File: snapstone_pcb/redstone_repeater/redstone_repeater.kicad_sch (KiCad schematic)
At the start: 17 parts, among them SW1 SW_Push, SW2 SW_Push, SW3 SW_Push, SW4 SW_Push, U1 MOUDLE-SEEEDUINO-XIAO, U2 Current Sensor

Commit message: Added almost all footprints
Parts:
- R1, R2, R3, R4, R5: footprint (none) -> Resistor_THT:R_Axial_DIN0309_L9.0mm_D3.2mm_P25.40mm_Horizontal
- SW1, SW2, SW3, SW4: footprint (none) -> Button_Switch_Keyboard:SW_Cherry_MX_1.00u_PCB
- U1: footprint (none) -> footprints:XIAO-Generic-Hybrid-14P-2.54-21X17.8MM
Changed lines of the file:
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@@
 			)
 		)
-		(property "Footprint" ""
+		(property "Footprint" "Resistor_THT:R_Axial_DIN0309_L9.0mm_D3.2mm_P25.40mm_Horizontal"
 			(at 193.294 84.074 90)
 			(effects
@@
 			)
 		)
-		(property "Footprint" ""
+		(property "Footprint" "Resistor_THT:R_Axial_DIN0309_L9.0mm_D3.2mm_P25.40mm_Horizontal"
 			(at 193.294 103.124 90)
 			(effects
@@
 			)
 		)
-		(property "Footprint" ""
+		(property "Footprint" "Resistor_THT:R_Axial_DIN0309_L9.0mm_D3.2mm_P25.40mm_Horizontal"
 			(at 193.294 65.024 90)
 			(effects
@@
 			)
 		)
-		(property "Footprint" ""
+		(property "Footprint" "Button_Switch_Keyboard:SW_Cherry_MX_1.00u_PCB"
 			(at 180.34 80.01 0)
 			(effects
@@
 			)
 		)
-		(property "Footprint" ""
+		(property "Footprint" "footprints:XIAO-Generic-Hybrid-14P-2.54-21X17.8MM"
 			(at 101.6 109.22 0)
 			(effects
@@
 			)
 		)
-		(property "Footprint" ""
+		(property "Footprint" "Resistor_THT:R_Axial_DIN0309_L9.0mm_D3.2mm_P25.40mm_Horizontal"
 			(at 119.126 72.136 90)
 			(effects
@@
 			)
 		)
-		(property "Footprint" ""
+		(property "Footprint" "Button_Switch_Keyboard:SW_Cherry_MX_1.00u_PCB"
 			(at 180.34 118.11 0)
 			(effects
@@
 			)
 		)
-		(property "Footprint" ""
+		(property "Footprint" "Resistor_THT:R_Axial_DIN0309_L9.0mm_D3.2mm_P25.40mm_Horizontal"
 			(at 193.294 122.174 90)
 			(effects
@@
 			)
 		)
-		(property "Footprint" ""
+		(property "Footprint" "Button_Switch_Keyboard:SW_Cherry_MX_1.00u_PCB"
 			(at 180.34 60.96 0)
 			(effects
@@
 			)
 		)
-		(property "Footprint" ""
+		(property "Footprint" "Button_Switch_Keyboard:SW_Cherry_MX_1.00u_PCB"
 			(at 180.34 99.06 0)
 			(effects

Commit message: All fottprints done schematic should be done
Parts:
- C1, C2, C3, C4: footprint (none) -> Capacitor_THT:CP_Radial_Tantal_D5.0mm_P2.50mm
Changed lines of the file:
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@@
 			)
 		)
-		(property "Footprint" ""
+		(property "Footprint" "Capacitor_THT:CP_Radial_Tantal_D5.0mm_P2.50mm"
 			(at 209.55 84.1248 0)
 			(effects
@@
 			)
 		)
-		(property "Footprint" ""
+		(property "Footprint" "Capacitor_THT:CP_Radial_Tantal_D5.0mm_P2.50mm"
 			(at 209.55 122.2248 0)
 			(effects
@@
 			)
 		)
-		(property "Footprint" ""
+		(property "Footprint" "Capacitor_THT:CP_Radial_Tantal_D5.0mm_P2.50mm"
 			(at 209.55 103.1748 0)
 			(effects
@@
 			)
 		)
-		(property "Footprint" ""
+		(property "Footprint" "Capacitor_THT:CP_Radial_Tantal_D5.0mm_P2.50mm"
 			(at 209.55 65.0748 0)
 			(effects

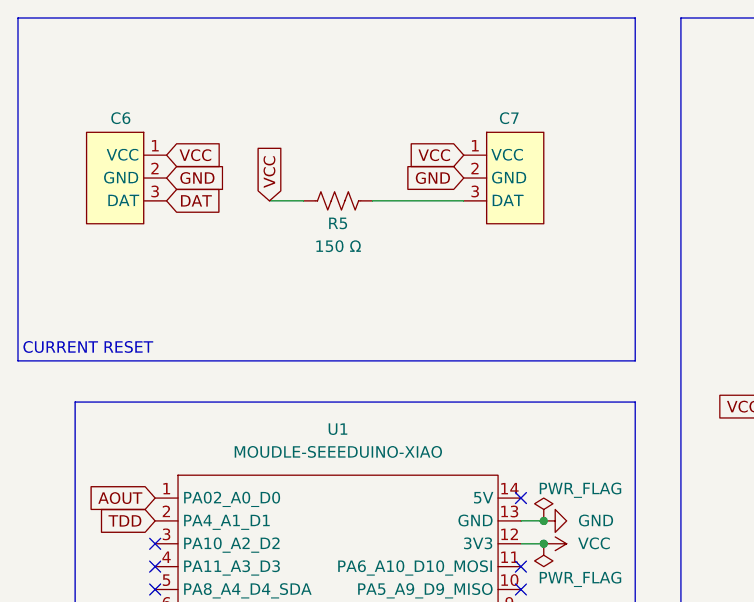
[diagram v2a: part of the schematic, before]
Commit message: Rerouted comparator wires to loop back into connector for inputs #1 and #2... and made some tiny style changes, lol.
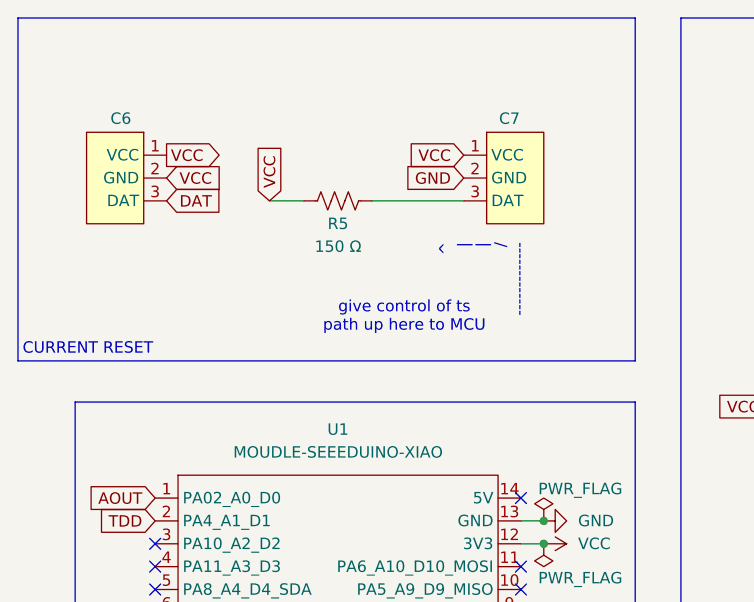
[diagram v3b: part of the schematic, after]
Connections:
- net GND: no longer C6.2 (GND)
- net VCC: now also C6.2 (GND)
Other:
- note added: "^ | | / -------------"
- note added: "give control of ts path up here to MCU"
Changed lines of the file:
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@@
+		)
+	)
+	(text "^\n|\n|\n/\n-------------  "
+		(exclude_from_sim no)
+		(at 135.382 75.946 90)
+		(effects
+			(font
+				(size 1.27 1.27)
+			)
+			(justify right)
 		)
 	)
@@
 		)
 	)
+	(text "give control of ts\npath up here to MCU"
+		(exclude_from_sim no)
+		(at 126.746 84.074 0)
+		(effects
+			(font
+				(size 1.27 1.27)
+			)
+		)
+	)
 	(text "MCU"
 		(exclude_from_sim no)
@@
 		)
 	)
+	(global_label "VCC"
+		(shape input)
+		(at 100.33 68.58 0)
+		(fields_autoplaced yes)
+		(effects
+			(font
+				(size 1.27 1.27)
+			)
+			(justify left)
+		)
+		(property "Intersheetrefs" "${INTERSHEET_REFS}"
+			(at 106.9438 68.58 0)
+			(effects
+				(font
+					(size 1.27 1.27)
+				)
+				(justify left)
+				(hide yes)
+			)
+		)
+	)
 	(global_label "TDD"
 		(shape input)
@@
 	)
 	(global_label "VCC"
-		(shape input)
+		(shape output)
 		(at 100.33 66.04 0)
 		(fields_autoplaced yes)
@@
 				(hide yes)
 			)
-		)
-	)
-	(global_label "GND"
-		(shape input)
-		(at 100.33 68.58 0)
-		(fields_autoplaced yes)
-		(effects
-			(font
-				(size 1.27 1.27)
-			)
-			(justify left)
-		)
-		(property "Intersheetrefs" "${INTERSHEET_REFS}"
-			(at 107.1857 68.58 0)
-			(effects
-				(font
-					(size 1.27 1.27)
-				)
-				(justify left)
-				(hide yes)
-			)

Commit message: Finished footprints and did all pcb in 30 mins somehow :sob:
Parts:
- C6, C7: footprint (none) -> TerminalBlock_4Ucon:TerminalBlock_4Ucon_1x03_P3.50mm_Horizontal
- U2: footprint TMCS1108A2UQDR_Current_Sensor:D0008A-IPC_A -> CurrentSensorSnap:D0008A-IPC_B
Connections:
- net DAT: now also U1.3 (PA10_A2_D2)
- net GND: no longer U2.4 (IN-)
- no-connect marks 13 -> 12
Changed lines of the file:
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@@
-	)
-	(no_connect
-		(at 99.06 109.22)
 	)
 	(no_connect
@@
 		(pts
 			(xy 185.42 85.09) (xy 189.23 85.09)
-		)
-		(stroke
-			(width 0)
-			(type default)
-		)
-	)
-	(wire
-		(pts
-			(xy 140.97 149.86) (xy 143.51 149.86)
 		)
 		(stroke
@@
 		)
 	)
-	(global_label "GND"
-		(shape input)
-		(at 105.41 160.02 180)
+	(global_label "TDD"
+		(shape output)
+		(at 199.39 69.85 270)
 		(fields_autoplaced yes)
 		(effects
@@
 		)
 		(property "Intersheetrefs" "${INTERSHEET_REFS}"
-			(at 98.5543 160.02 0)
+			(at 199.39 76.3428 90)
 			(effects
 				(font
@@
 		)
 	)
-	(global_label "TDD"
+	(global_label "VCC"
 		(shape output)
-		(at 199.39 69.85 270)
+		(at 100.33 66.04 0)
 		(fields_autoplaced yes)
 		(effects
@@
 				(size 1.27 1.27)
 			)
-			(justify right)
+			(justify left)
 		)
 		(property "Intersheetrefs" "${INTERSHEET_REFS}"
-			(at 199.39 76.3428 90)
-			(effects
-				(font
-					(size 1.27 1.27)
-				)
-				(justify right)
-				(hide yes)
-			)
-		)
-	)
-	(global_label "VCC"
-		(shape output)
-		(at 100.33 66.04 0)
+			(at 106.9438 66.04 0)
+			(effects
+				(font
+					(size 1.27 1.27)
+				)
+				(justify left)
+				(hide yes)
+			)
+		)
+	)
+	(global_label "AOUT"
+		(shape input)
+		(at 99.06 104.14 180)
 		(fields_autoplaced yes)
 		(effects
@@
 				(size 1.27 1.27)
 			)
-			(justify left)
+			(justify right)
 		)
 		(property "Intersheetrefs" "${INTERSHEET_REFS}"
-			(at 106.9438 66.04 0)
-			(effects
-				(font
-					(size 1.27 1.27)
-				)
-				(justify left)
-				(hide yes)
-			)
-		)
-	)
-	(global_label "AOUT"
+			(at 91.3576 104.14 0)
+			(effects
+				(font
+					(size 1.27 1.27)
+				)
+				(justify right)
+				(hide yes)
+			)
+		)
+	)
+	(global_label "VCC"
 		(shape input)
-		(at 99.06 104.14 180)
+		(at 167.64 93.98 180)
 		(fields_autoplaced yes)
 		(effects
@@
 		)
 		(property "Intersheetrefs" "${INTERSHEET_REFS}"
-			(at 91.3576 104.14 0)
+			(at 161.0262 93.98 0)
 			(effects
 				(font
@@
 		)
 	)
-	(global_label "VCC"
+	(global_label "DAT"
 		(shape input)
-		(at 167.64 93.98 180)
+		(at 105.41 144.78 180)
 		(fields_autoplaced yes)
 		(effects
@@
 		)
 		(property "Intersheetrefs" "${INTERSHEET_REFS}"
-			(at 161.0262 93.98 0)
+			(at 99.0986 144.78 0)
 			(effects
 				(font
@@
 		)
 	)
-	(global_label "DAT"
-		(shape input)
-		(at 105.41 144.78 180)
+	(global_label "TDD"
+		(shape output)
+		(at 199.39 127 270)
 		(fields_autoplaced yes)
 		(effects
@@
 		)
 		(property "Intersheetrefs" "${INTERSHEET_REFS}"
-			(at 99.0986 144.78 0)
+			(at 199.39 133.4928 90)
 			(effects
 				(font
@@
 		)
 	)
-	(global_label "TDD"
-		(shape output)
-		(at 199.39 127 270)
+	(global_label "DAT"
+		(shape input)
+		(at 99.06 109.22 180)
 		(fields_autoplaced yes)
 		(effects
@@
 		)
 		(property "Intersheetrefs" "${INTERSHEET_REFS}"
-			(at 199.39 133.4928 90)
+			(at 92.7486 109.22 0)
 			(effects
 				(font
@@
 	(global_label "AOUT"
 		(shape output)
-		(at 143.51 149.86 0)
+		(at 140.97 149.86 0)
 		(fields_autoplaced yes)
 		(effects
@@
 		)
 		(property "Intersheetrefs" "${INTERSHEET_REFS}"
-			(at 151.2124 149.86 0)
+			(at 148.6724 149.86 0)
 			(effects
 				(font
@@
 			)
 		)
-		(property "Footprint" ""
+		(property "Footprint" "TerminalBlock_4Ucon:TerminalBlock_4Ucon_1x03_P3.50mm_Horizontal"
 			(at 138.43 73.66 0)
 			(effects
@@
 			)
 		)
-		(property "Footprint" ""
+		(property "Footprint" "TerminalBlock_4Ucon:TerminalBlock_4Ucon_1x03_P3.50mm_Horizontal"
 			(at 95.25 73.66 0)
 			(effects
@@
 			)
 		)
-		(property "Footprint" "TMCS1108A2UQDR_Current_Sensor:D0008A-IPC_A"
+		(property "Footprint" "CurrentSensorSnap:D0008A-IPC_B"
 			(at 105.41 144.78 0)
 			(effects

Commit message: did a bunch of stuff (something something Redstone Repeater PCB Changes)
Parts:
- C_IN1: renamed from C6; footprint TerminalBlock_4Ucon:TerminalBlock_4Ucon_1x03_P3.50mm_Horizontal -> 691137710003_Board_To_Wire:691137710003_Board_To_Wire
- C_OUT1: renamed from C7; footprint TerminalBlock_4Ucon:TerminalBlock_4Ucon_1x03_P3.50mm_Horizontal -> 691137710003_Board_To_Wire:691137710003_Board_To_Wire
- R1, R2, R3, R4, R5: footprint Resistor_THT:R_Axial_DIN0309_L9.0mm_D3.2mm_P25.40mm_Horizontal -> CF12JT150R_Resistor_150:STA_CF12_STP
- U2: footprint CurrentSensorSnap:D0008A-IPC_B -> TMCS1108A2UQDR_Current_Sensor:D0008A-IPC_A
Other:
- note removed: "^ | | / -------------"
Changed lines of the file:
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@@
-		)
-	)
-	(text "^\n|\n|\n/\n-------------  "
-		(exclude_from_sim no)
-		(at 135.382 75.946 90)
-		(effects
-			(font
-				(size 1.27 1.27)
-			)
-			(justify right)
 		)
 	)
@@
 		(on_board yes)
 		(dnp no)
-		(property "Reference" "C7"
-			(at 138.43 61.976 0)
+		(property "Reference" "C_OUT1"
+			(at 139.192 61.722 0)
 			(effects
 				(font
@@
 			)
 		)
-		(property "Footprint" "TerminalBlock_4Ucon:TerminalBlock_4Ucon_1x03_P3.50mm_Horizontal"
+		(property "Footprint" "691137710003_Board_To_Wire:691137710003_Board_To_Wire"
 			(at 138.43 73.66 0)
 			(effects
@@
 			(project "redstone_repeater"
 				(path "/c6e4f295-c396-42f7-a6d5-97e88b8cc9c0"
-					(reference "C7")
+					(reference "C_OUT1")
 					(unit 1)
 				)
@@
 			)
 		)
-		(property "Footprint" "Resistor_THT:R_Axial_DIN0309_L9.0mm_D3.2mm_P25.40mm_Horizontal"
+		(property "Footprint" "CF12JT150R_Resistor_150:STA_CF12_STP"
 			(at 193.294 84.074 90)
 			(effects
@@
 			)
 		)
-		(property "Footprint" "Resistor_THT:R_Axial_DIN0309_L9.0mm_D3.2mm_P25.40mm_Horizontal"
+		(property "Footprint" "CF12JT150R_Resistor_150:STA_CF12_STP"
 			(at 193.294 103.124 90)
 			(effects
@@
 			)
 		)
-		(property "Footprint" "Resistor_THT:R_Axial_DIN0309_L9.0mm_D3.2mm_P25.40mm_Horizontal"
+		(property "Footprint" "CF12JT150R_Resistor_150:STA_CF12_STP"
 			(at 193.294 65.024 90)
 			(effects
@@
 		(on_board yes)
 		(dnp no)
-		(property "Reference" "C6"
-			(at 95.25 61.976 0)
+		(property "Reference" "C_IN1"
+			(at 94.488 61.722 0)
 			(effects
 				(font
@@
 			)
 		)
-		(property "Footprint" "TerminalBlock_4Ucon:TerminalBlock_4Ucon_1x03_P3.50mm_Horizontal"
+		(property "Footprint" "691137710003_Board_To_Wire:691137710003_Board_To_Wire"
 			(at 95.25 73.66 0)
 			(effects
@@
 			(project "redstone_repeater"
 				(path "/c6e4f295-c396-42f7-a6d5-97e88b8cc9c0"
-					(reference "C6")
+					(reference "C_IN1")
 					(unit 1)
 				)
@@
 			)
 		)
-		(property "Footprint" "Resistor_THT:R_Axial_DIN0309_L9.0mm_D3.2mm_P25.40mm_Horizontal"
+		(property "Footprint" "CF12JT150R_Resistor_150:STA_CF12_STP"
 			(at 119.126 72.136 90)
 			(effects
@@
 			)
 		)
-		(property "Footprint" "Resistor_THT:R_Axial_DIN0309_L9.0mm_D3.2mm_P25.40mm_Horizontal"
+		(property "Footprint" "CF12JT150R_Resistor_150:STA_CF12_STP"
 			(at 193.294 122.174 90)
 			(effects
@@
 			)
 		)
-		(property "Footprint" "CurrentSensorSnap:D0008A-IPC_B"
+		(property "Footprint" "TMCS1108A2UQDR_Current_Sensor:D0008A-IPC_A"
 			(at 105.41 144.78 0)
 			(effects

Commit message: Updated resistor footprint project-wide
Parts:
- C_IN1, C_OUT1: value ~ -> (none)
- R1, R2, R3, R4, R5: footprint CF12JT150R_Resistor_150:STA_CF12_STP -> CF12JT_Resistor:STA_CF12_STP
